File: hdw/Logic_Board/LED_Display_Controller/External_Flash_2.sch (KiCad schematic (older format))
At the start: 16 parts, among them U1901 SST25PF020B

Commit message: Added some digikey partnumbers to components
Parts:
- C1901: footprint (none) -> Capacitors_SMD:C_0603; Digi-Key PN PN -> 311-1344-1-ND; Voltage 25V -> 50V
- C1902: Digi-Key PN PN -> 1276-1921-1-ND; Voltage 25V -> 50V
- C1903: Digi-Key PN PN -> 1276-1018-1-ND; Voltage 25V -> 50V
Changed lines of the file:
@@
 F 0 "C1901" H 5815 5530 50  0000 L CNN
 F 1 "0.1uF" H 5815 5330 50  0000 L CNN
-F 2 "" H 5828 5280 50  0001 C CNN
+F 2 "Capacitors_SMD:C_0603" H 5828 5280 50  0001 C CNN
 F 3 "" H 5815 5530 50  0001 C CNN
 F 4 "0603" H 5640 5530 50  0000 R CNN "display_footprint"
-F 5 "25V" H 5640 5430 50  0000 R CNN "Voltage"
+F 5 "50V" H 5640 5430 50  0000 R CNN "Voltage"
 F 6 "X7R" H 5640 5330 50  0000 R CNN "Dielectric"
-F 7 "PN" H 6215 5930 60  0001 C CNN "Digi-Key PN"
+F 7 "311-1344-1-ND" H 6215 5930 60  0001 C CNN "Digi-Key PN"
 	1    5790 5430
 	1    0    0    -1
@@
 F 3 "" H 6115 5530 50  0001 C CNN
 F 4 "0603" H 5940 5530 50  0001 R CNN "display_footprint"
-F 5 "25V" H 5940 5430 50  0001 R CNN "Voltage"
+F 5 "50V" H 5940 5430 50  0001 R CNN "Voltage"
 F 6 "X7R" H 5940 5330 50  0001 R CNN "Dielectric"
-F 7 "PN" H 6515 5930 60  0001 C CNN "Digi-Key PN"
+F 7 "1276-1921-1-ND" H 6515 5930 60  0001 C CNN "Digi-Key PN"
 	1    6090 5430
 	1    0    0    -1
@@
 F 3 "" H 6415 5530 50  0001 C CNN
 F 4 "0603" H 6240 5530 50  0001 R CNN "display_footprint"
-F 5 "25V" H 6240 5430 50  0001 R CNN "Voltage"
+F 5 "50V" H 6240 5430 50  0001 R CNN "Voltage"
 F 6 "X7R" H 6240 5330 50  0001 R CNN "Dielectric"
-F 7 "PN" H 6815 5930 60  0001 C CNN "Digi-Key PN"
+F 7 "1276-1018-1-ND" H 6815 5930 60  0001 C CNN "Digi-Key PN"
 	1    6390 5430
 	1    0    0    -1

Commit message: Finished first pass of digikey part numbers
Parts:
- R1901, R1902, R1903, R1904, R1905, R1912: Digi-Key PN PN -> A106047CT-ND
- R1906, R1907, R1908, R1909, R1910, R1911: Digi-Key PN PN -> RMCF0603FT10K0CT-ND
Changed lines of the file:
@@
 F 5 "1%" H 5410 4320 50  0000 L CNN "Tolerance"
 F 6 "1/10W" H 5410 4240 50  0000 L CNN "Wattage"
-F 7 "PN" H 5630 4720 60  0001 C CNN "Digi-Key PN"
+F 7 "RMCF0603FT10K0CT-ND" H 5630 4720 60  0001 C CNN "Digi-Key PN"
 	1    5330 4320
 	1    0    0    -1
@@
 F 5 "1%" H 4600 4320 50  0000 L CNN "Tolerance"
 F 6 "1/10W" H 4600 4240 50  0000 L CNN "Wattage"
-F 7 "PN" H 4820 4720 60  0001 C CNN "Digi-Key PN"
+F 7 "RMCF0603FT10K0CT-ND" H 4820 4720 60  0001 C CNN "Digi-Key PN"
 	1    4520 4320
 	1    0    0    -1
@@
 F 5 "1%" H 5190 3130 50  0000 L CNN "Tolerance"
 F 6 "1/10W" H 5190 3050 50  0000 L CNN "Wattage"
-F 7 "PN" H 5410 3530 60  0001 C CNN "Digi-Key PN"
+F 7 "RMCF0603FT10K0CT-ND" H 5410 3530 60  0001 C CNN "Digi-Key PN"
 	1    5110 3130
 	1    0    0    -1
@@
 F 5 "1%" H 4600 3130 50  0000 L CNN "Tolerance"
 F 6 "1/10W" H 4600 3050 50  0000 L CNN "Wattage"
-F 7 "PN" H 4820 3530 60  0001 C CNN "Digi-Key PN"
+F 7 "RMCF0603FT10K0CT-ND" H 4820 3530 60  0001 C CNN "Digi-Key PN"
 	1    4520 3130
 	1    0    0    -1
@@
 F 5 "1%" H 4010 3130 50  0000 L CNN "Tolerance"
 F 6 "1/10W" H 4010 3050 50  0000 L CNN "Wattage"
-F 7 "PN" H 4230 3530 60  0001 C CNN "Digi-Key PN"
+F 7 "RMCF0603FT10K0CT-ND" H 4230 3530 60  0001 C CNN "Digi-Key PN"
 	1    3930 3130
 	1    0    0    -1
@@
 F 5 "1%" H 6830 3850 50  0000 L CNN "Tolerance"
 F 6 "1/10W" H 6830 3770 50  0000 L CNN "Wattage"
-F 7 "PN" H 7050 4250 60  0001 C CNN "Digi-Key PN"
+F 7 "RMCF0603FT10K0CT-ND" H 7050 4250 60  0001 C CNN "Digi-Key PN"
 	1    6750 3850
 	1    0    0    -1
@@
 F 5 "1%" V 3620 3450 50  0001 C CNN "Tolerance"
 F 6 "1/10W" V 3720 3450 50  0001 C CNN "Wattage"
-F 7 "PN" H 3720 3850 60  0001 C CNN "Digi-Key PN"
+F 7 "A106047CT-ND" H 3720 3850 60  0001 C CNN "Digi-Key PN"
 	1    3420 3450
 	0    1    1    0
@@
 F 5 "1%" V 7330 3450 50  0001 C CNN "Tolerance"
 F 6 "1/10W" V 7430 3450 50  0001 C CNN "Wattage"
-F 7 "PN" H 7430 3850 60  0001 C CNN "Digi-Key PN"
+F 7 "A106047CT-ND" H 7430 3850 60  0001 C CNN "Digi-Key PN"
 	1    7130 3450
 	0    1    1    0
@@
 F 5 "1%" V 3620 3550 50  0001 C CNN "Tolerance"
 F 6 "1/10W" V 3720 3550 50  0001 C CNN "Wattage"
-F 7 "PN" H 3720 3950 60  0001 C CNN "Digi-Key PN"
+F 7 "A106047CT-ND" H 3720 3950 60  0001 C CNN "Digi-Key PN"
 	1    3420 3550
 	0    1    1    0
@@
 F 5 "1%" V 3620 3750 50  0001 C CNN "Tolerance"
 F 6 "1/10W" V 3720 3750 50  0001 C CNN "Wattage"
-F 7 "PN" H 3720 4150 60  0001 C CNN "Digi-Key PN"
+F 7 "A106047CT-ND" H 3720 4150 60  0001 C CNN "Digi-Key PN"
 	1    3420 3750
 	0    1    1    0
@@
 F 5 "1%" V 3620 3850 50  0001 C CNN "Tolerance"
 F 6 "1/10W" V 3720 3850 50  0001 C CNN "Wattage"
-F 7 "PN" H 3720 4250 60  0001 C CNN "Digi-Key PN"
+F 7 "A106047CT-ND" H 3720 4250 60  0001 C CNN "Digi-Key PN"
 	1    3420 3850
 	0    1    1    0
@@
 F 5 "1%" V 3620 3650 50  0001 C CNN "Tolerance"
 F 6 "1/10W" V 3720 3650 50  0001 C CNN "Wattage"
-F 7 "PN" H 3720 4050 60  0001 C CNN "Digi-Key PN"
+F 7 "A106047CT-ND" H 3720 4050 60  0001 C CNN "Digi-Key PN"
 	1    3420 3650
 	0    1    1    0

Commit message: First pass assignment of footprints to all components
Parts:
- C1902, C1903: footprint (none) -> Capacitors_SMD:C_0603
- R1901, R1902, R1903, R1904, R1905, R1906, R1907, R1908, R1909, R1910, R1911, R1912: footprint (none) -> Resistors_SMD:R_0603
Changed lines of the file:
@@
 F 0 "R1910" H 5270 4320 50  0000 R CNN
 F 1 "10k" V 5330 4320 50  0000 C CNN
-F 2 "" H 5330 4320 50  0001 C CNN
+F 2 "Resistors_SMD:R_0603" H 5330 4320 50  0001 C CNN
 F 3 "" H 5330 4320 50  0001 C CNN
 F 4 "0603" H 5410 4400 50  0000 L CNN "display_footprint"
@@
 F 0 "R1908" H 4460 4320 50  0000 R CNN
 F 1 "10k" V 4520 4320 50  0000 C CNN
-F 2 "" H 4520 4320 50  0001 C CNN
+F 2 "Resistors_SMD:R_0603" H 4520 4320 50  0001 C CNN
 F 3 "" H 4520 4320 50  0001 C CNN
 F 4 "0603" H 4600 4400 50  0000 L CNN "display_footprint"
@@
 F 0 "R1909" H 5050 3130 50  0000 R CNN
 F 1 "10k" V 5110 3130 50  0000 C CNN
-F 2 "" H 5110 3130 50  0001 C CNN
+F 2 "Resistors_SMD:R_0603" H 5110 3130 50  0001 C CNN
 F 3 "" H 5110 3130 50  0001 C CNN
 F 4 "0603" H 5190 3210 50  0000 L CNN "display_footprint"
@@
 F 0 "R1907" H 4460 3130 50  0000 R CNN
 F 1 "10k" V 4520 3130 50  0000 C CNN
-F 2 "" H 4520 3130 50  0001 C CNN
+F 2 "Resistors_SMD:R_0603" H 4520 3130 50  0001 C CNN
 F 3 "" H 4520 3130 50  0001 C CNN
 F 4 "0603" H 4600 3210 50  0000 L CNN "display_footprint"
@@
 F 0 "R1906" H 3870 3130 50  0000 R CNN
 F 1 "10k" V 3930 3130 50  0000 C CNN
-F 2 "" H 3930 3130 50  0001 C CNN
+F 2 "Resistors_SMD:R_0603" H 3930 3130 50  0001 C CNN
 F 3 "" H 3930 3130 50  0001 C CNN
 F 4 "0603" H 4010 3210 50  0000 L CNN "display_footprint"
@@
 F 0 "R1911" H 6690 3850 50  0000 R CNN
 F 1 "10k" V 6750 3850 50  0000 C CNN
-F 2 "" H 6750 3850 50  0001 C CNN
+F 2 "Resistors_SMD:R_0603" H 6750 3850 50  0001 C CNN
 F 3 "" H 6750 3850 50  0001 C CNN
 F 4 "0603" H 6830 3930 50  0000 L CNN "display_footprint"
@@
 F 0 "R1901" V 3380 3580 50  0000 L CNN
 F 1 "100" V 3420 3450 50  0000 C CNN
-F 2 "" H 3420 3450 50  0001 C CNN
+F 2 "Resistors_SMD:R_0603" H 3420 3450 50  0001 C CNN
 F 3 "" H 3420 3450 50  0001 C CNN
 F 4 "0603" V 3520 3450 50  0001 C CNN "display_footprint"
@@
 F 0 "R1912" V 7030 3450 50  0000 C CNN
 F 1 "100" V 7130 3450 50  0000 C CNN
-F 2 "" H 7130 3450 50  0001 C CNN
+F 2 "Resistors_SMD:R_0603" H 7130 3450 50  0001 C CNN
 F 3 "" H 7130 3450 50  0001 C CNN
 F 4 "0603" V 7230 3450 50  0001 C CNN "display_footprint"
@@
 F 0 "C1902" H 6115 5530 50  0000 L CNN
 F 1 "10nF" H 6115 5330 50  0000 L CNN
-F 2 "" H 6128 5280 50  0001 C CNN
+F 2 "Capacitors_SMD:C_0603" H 6128 5280 50  0001 C CNN
 F 3 "" H 6115 5530 50  0001 C CNN
 F 4 "0603" H 5940 5530 50  0001 R CNN "display_footprint"
@@
 F 0 "C1903" H 6415 5530 50  0000 L CNN
 F 1 "1nF" H 6415 5330 50  0000 L CNN
-F 2 "" H 6428 5280 50  0001 C CNN
+F 2 "Capacitors_SMD:C_0603" H 6428 5280 50  0001 C CNN
 F 3 "" H 6415 5530 50  0001 C CNN
 F 4 "0603" H 6240 5530 50  0001 R CNN "display_footprint"
@@
 F 0 "R1902" V 3380 3680 50  0000 L CNN
 F 1 "100" V 3420 3550 50  0000 C CNN
-F 2 "" H 3420 3550 50  0001 C CNN
+F 2 "Resistors_SMD:R_0603" H 3420 3550 50  0001 C CNN
 F 3 "" H 3420 3550 50  0001 C CNN
 F 4 "0603" V 3520 3550 50  0001 C CNN "display_footprint"
@@
 F 0 "R1904" V 3380 3880 50  0000 L CNN
 F 1 "100" V 3420 3750 50  0000 C CNN
-F 2 "" H 3420 3750 50  0001 C CNN
+F 2 "Resistors_SMD:R_0603" H 3420 3750 50  0001 C CNN
 F 3 "" H 3420 3750 50  0001 C CNN
 F 4 "0603" V 3520 3750 50  0001 C CNN "display_footprint"
@@
 F 0 "R1905" V 3380 3980 50  0000 L CNN
 F 1 "100" V 3420 3850 50  0000 C CNN
-F 2 "" H 3420 3850 50  0001 C CNN
+F 2 "Resistors_SMD:R_0603" H 3420 3850 50  0001 C CNN
 F 3 "" H 3420 3850 50  0001 C CNN
 F 4 "0603" V 3520 3850 50  0001 C CNN "display_footprint"
@@
 F 0 "R1903" V 3380 3780 50  0000 L CNN
 F 1 "100" V 3420 3650 50  0000 C CNN
-F 2 "" H 3420 3650 50  0001 C CNN
+F 2 "Resistors_SMD:R_0603" H 3420 3650 50  0001 C CNN
 F 3 "" H 3420 3650 50  0001 C CNN
 F 4 "0603" V 3520 3650 50  0001 C CNN "display_footprint"

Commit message: Resolved a few library dependencies
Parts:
- R1901, R1902, R1903, R1904, R1905, R1906, R1907, R1908, R1909, R1910, R1911, R1912: symbol Custom_Library:R_Custom -> LED_Display_Local_Library:R_Custom
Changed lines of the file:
@@
 $EndComp
 $Comp
-L Custom_Library:R_Custom R?
+L LED_Display_Local_Library:R_Custom R?
 U 1 1 5BBE78FD
 P 5330 4320
@@
 $EndComp
 $Comp
-L Custom_Library:R_Custom R?
+L LED_Display_Local_Library:R_Custom R?
 U 1 1 5BBE7908
 P 4520 4320
@@
 $EndComp
 $Comp
-L Custom_Library:R_Custom R?
+L LED_Display_Local_Library:R_Custom R?
 U 1 1 5BBE7913
 P 5110 3130
@@
 $EndComp
 $Comp
-L Custom_Library:R_Custom R?
+L LED_Display_Local_Library:R_Custom R?
 U 1 1 5BBE791E
 P 4520 3130
@@
 $EndComp
 $Comp
-L Custom_Library:R_Custom R?
+L LED_Display_Local_Library:R_Custom R?
 U 1 1 5BBE7929
 P 3930 3130
@@
 $EndComp
 $Comp
-L Custom_Library:R_Custom R?
+L LED_Display_Local_Library:R_Custom R?
 U 1 1 5BBE7934
 P 6750 3850
@@
 $EndComp
 $Comp
-L Custom_Library:R_Custom R?
+L LED_Display_Local_Library:R_Custom R?
 U 1 1 5BBE7963
 P 3420 3450
@@
 FLASH_SCK
 $Comp
-L Custom_Library:R_Custom R?
+L LED_Display_Local_Library:R_Custom R?
 U 1 1 5BBE7990
 P 7130 3450
@@
 	6090 5240 6390 5240
 $Comp
-L Custom_Library:R_Custom R?
+L LED_Display_Local_Library:R_Custom R?
 U 1 1 5BBE79DB
 P 3420 3550
@@
 $EndComp
 $Comp
-L Custom_Library:R_Custom R?
+L LED_Display_Local_Library:R_Custom R?
 U 1 1 5BBE79E6
 P 3420 3750
@@
 $EndComp
 $Comp
-L Custom_Library:R_Custom R?
+L LED_Display_Local_Library:R_Custom R?
 U 1 1 5BBE79F1
 P 3420 3850
@@
 ~FLASH_Hold
 $Comp
-L Custom_Library:R_Custom R1903
+L LED_Display_Local_Library:R_Custom R1903
 U 1 1 5BC1C038
 P 3420 3650

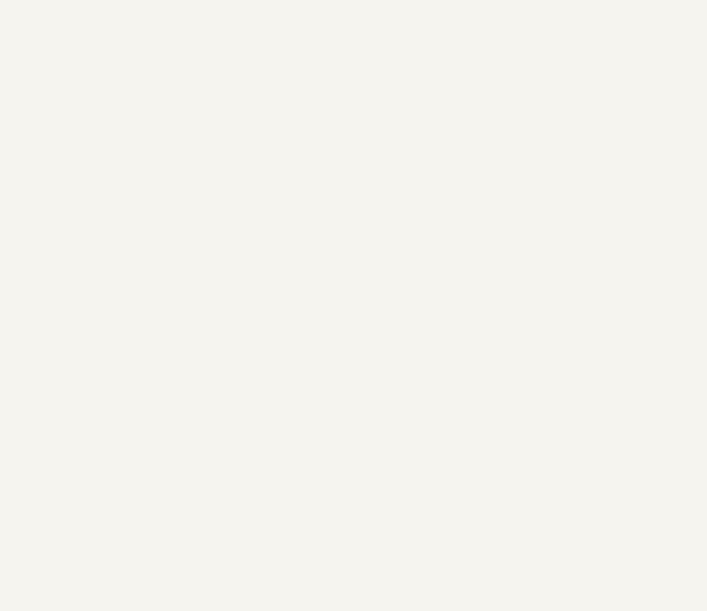
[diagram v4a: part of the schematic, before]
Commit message: Added flash chip select LEDs
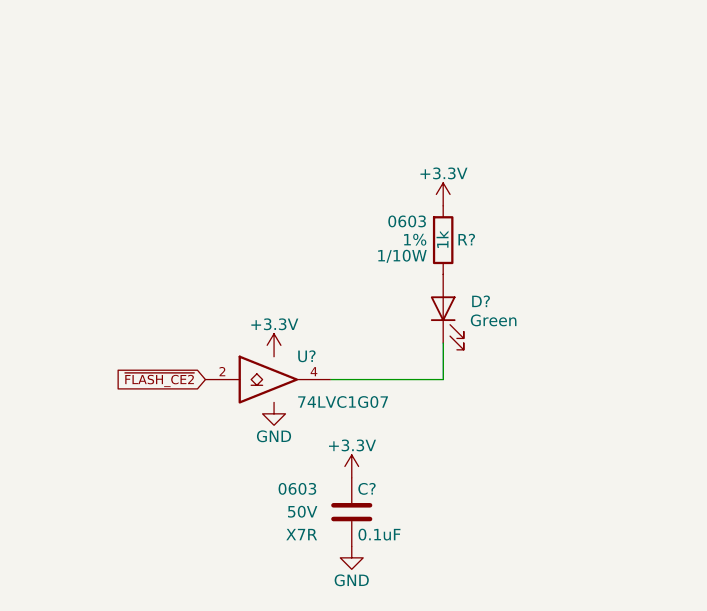
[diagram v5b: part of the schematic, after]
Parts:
- added C?: 0.1uF, Capacitors_SMD:C_0603, symbol LED_Display_Local_Library:C_Custom
- added D?: Green, LEDs:LED_0603, symbol Device:LED
- added R?: 1k, Resistors_SMD:R_0603, symbol LED_Display_Local_Library:R_Custom
- added U?: 74LVC1G07, TO_SOT_Packages_SMD:SOT-353_SC-70-5, symbol LED_Display_Local_Library:74LVC1G07_Power
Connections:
- net +3V3: now also C?.1, R?.1, U?.5 (VCC)
- net GND: now also C?.2, U?.3 (GND)
- net ~FLASH_CE2: now also U?.2
- new net: D?.1 (K), U?.4
- new net: D?.2 (A), R?.2
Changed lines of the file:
@@
 Wire Wire Line
 	4520 3850 5680 3850
+$Comp
+L LED_Display_Local_Library:C_Custom C?
+U 1 1 5C17189B
+P 2010 6900
+AR Path="/5BAAE16C/5C17189B" Ref="C?"  Part="1"
+AR Path="/5BB181D8/5C17189B" Ref="C?"  Part="1"
+AR Path="/5BB2595E/5C17189B" Ref="C?"  Part="1"
+AR Path="/5BB25AE7/5C17189B" Ref="C?"  Part="1"
+F 0 "C?" H 2035 7000 50  0000 L CNN
+F 1 "0.1uF" H 2035 6800 50  0000 L CNN
+F 2 "Capacitors_SMD:C_0603" H 2048 6750 50  0001 C CNN
+F 3 "" H 2035 7000 50  0001 C CNN
+F 4 "0603" H 1860 7000 50  0000 R CNN "display_footprint"
+F 5 "50V" H 1860 6900 50  0000 R CNN "Voltage"
+F 6 "X7R" H 1860 6800 50  0000 R CNN "Dielectric"
+F 7 "311-1344-1-ND" H 2435 7400 60  0001 C CNN "Digi-Key PN"
+	1    2010 6900
+	1    0    0    -1
+$EndComp
+$Comp
+L LED_Display_Local_Library:74LVC1G07_Power U?
+U 1 1 5C1718A3
+P 1670 6320
+AR Path="/5BB2595E/5C1718A3" Ref="U?"  Part="1"
+AR Path="/5BB25AE7/5C1718A3" Ref="U?"  Part="1"
+F 0 "U?" H 1770 6420 50  0000 L CNN
+F 1 "74LVC1G07" H 1770 6220 50  0000 L CNN
+F 2 "TO_SOT_Packages_SMD:SOT-353_SC-70-5" H 1670 6320 50  0001 C CNN
+F 3 "http://www.ti.com/lit/sg/scyt129e/scyt129e.pdf" H 1670 6320 50  0001 C CNN
+F 4 "296-8486-1-ND" H 1670 6320 50  0001 C CNN "Digi-Key PN"
+	1    1670 6320
+	1    0    0    -1
+$EndComp
+$Comp
+L power:+3.3V #PWR?
+U 1 1 5C1718AA
+P 1670 6220
+AR Path="/5BB2595E/5C1718AA" Ref="#PWR?"  Part="1"
+AR Path="/5BB25AE7/5C1718AA" Ref="#PWR?"  Part="1"
+F 0 "#PWR?" H 1670 6070 50  0001 C CNN
+F 1 "+3.3V" H 1670 6360 50  0000 C CNN
+F 2 "" H 1670 6220 50  0001 C CNN
+F 3 "" H 1670 6220 50  0001 C CNN
+	1    1670 6220
+	1    0    0    -1
+$EndComp
+$Comp
+L power:+3.3V #PWR?
+U 1 1 5C1718B0
+P 2010 6750
+AR Path="/5BB2595E/5C1718B0" Ref="#PWR?"  Part="1"
+AR Path="/5BB25AE7/5C1718B0" Ref="#PWR?"  Part="1"
+F 0 "#PWR?" H 2010 6600 50  0001 C CNN
+F 1 "+3.3V" H 2010 6890 50  0000 C CNN
+F 2 "" H 2010 6750 50  0001 C CNN
+F 3 "" H 2010 6750 50  0001 C CNN
+	1    2010 6750
+	1    0    0    -1
+$EndComp
+$Comp
+L power:GND #PWR?
+U 1 1 5C1718B6
+P 2010 7050
+AR Path="/5BB2595E/5C1718B6" Ref="#PWR?"  Part="1"
+AR Path="/5BB25AE7/5C1718B6" Ref="#PWR?"  Part="1"
+F 0 "#PWR?" H 2010 6800 50  0001 C CNN
+F 1 "GND" H 2010 6900 50  0000 C CNN
+F 2 "" H 2010 7050 50  0001 C CNN
+F 3 "" H 2010 7050 50  0001 C CNN
+	1    2010 7050
+	1    0    0    -1
+$EndComp
+$Comp
+L power:GND #PWR?
+U 1 1 5C1718BC
+P 1670 6420
+AR Path="/5BB2595E/5C1718BC" Ref="#PWR?"  Part="1"
+AR Path="/5BB25AE7/5C1718BC" Ref="#PWR?"  Part="1"
+F 0 "#PWR?" H 1670 6170 50  0001 C CNN
+F 1 "GND" H 1670 6270 50  0000 C CNN
+F 2 "" H 1670 6420 50  0001 C CNN
+F 3 "" H 1670 6420 50  0001 C CNN
+	1    1670 6420
+	1    0    0    -1
+$EndComp
+Text GLabel 1370 6320 0    40   Input ~ 0
+~FLASH_CE2
+$Comp
+L power:+3.3V #PWR?
+U 1 1 5C1718C3
+P 2410 5560
+AR Path="/5BB844FD/5C1718C3" Ref="#PWR?"  Part="1"
+AR Path="/5BF346B3/5C1718C3" Ref="#PWR?"  Part="1"
+AR Path="/5BB2595E/5C1718C3" Ref="#PWR?"  Part="1"
+AR Path="/5BB25AE7/5C1718C3" Ref="#PWR?"  Part="1"
+F 0 "#PWR?" H 2410 5410 50  0001 C CNN
+F 1 "+3.3V" H 2410 5700 50  0000 C CNN
+F 2 "" H 2410 5560 50  0001 C CNN
+F 3 "" H 2410 5560 50  0001 C CNN
+	1    2410 5560
+	1    0    0    -1
+$EndComp
+Wire Wire Line
+	1920 6320 2410 6320
+Wire Wire Line
+	2410 6320 2410 6160
+$Comp
+L LED_Display_Local_Library:R_Custom R?
+U 1 1 5C1718CF
+P 2410 5710
+AR Path="/5BAAE1F3/5C1718CF" Ref="R?"  Part="1"
+AR Path="/5BAAE1DC/5C1718CF" Ref="R?"  Part="1"
+AR Path="/5BAAE16C/5C1718CF" Ref="R?"  Part="1"
+AR Path="/5BB844FD/5C1718CF" Ref="R?"  Part="1"
+AR Path="/5BF346B3/5C1718CF" Ref="R?"  Part="1"
+AR Path="/5BB2595E/5C1718CF" Ref="R?"  Part="1"
+AR Path="/5BB25AE7/5C1718CF" Ref="R?"  Part="1"
+F 0 "R?" H 2350 5710 50  0000 R CNN
+F 1 "1k" V 2410 5710 50  0000 C CNN
+F 2 "Resistors_SMD:R_0603" H 2410 5710 50  0001 C CNN
+F 3 "" H 2410 5710 50  0001 C CNN
+F 4 "0603" H 2480 5790 50  0000 L CNN "display_footprint"
+F 5 "1%" H 2480 5710 50  0000 L CNN "Tolerance"
+F 6 "1/10W" H 2480 5640 50  0000 L CNN "Wattage"
+F 7 "RMCF0603FT1K00CT-ND" H 2710 6110 60  0001 C CNN "Digi-Key PN"
+	1    2410 5710
+	-1   0    0    -1
+$EndComp
+$Comp
+L Device:LED D?
+U 1 1 5C1718D7
+P 2410 6010
+AR Path="/5BB844FD/5C1718D7" Ref="D?"  Part="1"
+AR Path="/5BF346B3/5C1718D7" Ref="D?"  Part="1"
+AR Path="/5BB2595E/5C1718D7" Ref="D?"  Part="1"
+AR Path="/5BB25AE7/5C1718D7" Ref="D?"  Part="1"
+F 0 "D?" V 2440 5890 50  0000 R CNN
+F 1 "Green" V 2357 5893 50  0000 R CNN
+F 2 "LEDs:LED_0603" H 2410 6010 50  0001 C CNN
+F 3 "~" H 2410 6010 50  0001 C CNN
+F 4 "160-1446-1-ND" H -2600 3010 50  0001 C CNN "Digi-Key PN"
+	1    2410 6010
+	0    -1   -1   0
+$EndComp
 $EndSCHEMATC

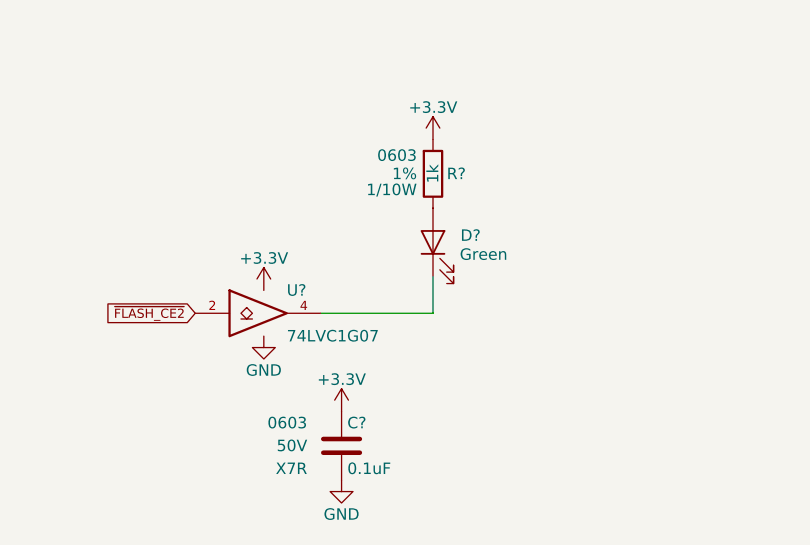
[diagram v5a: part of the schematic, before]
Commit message: Added WIFI comm LED
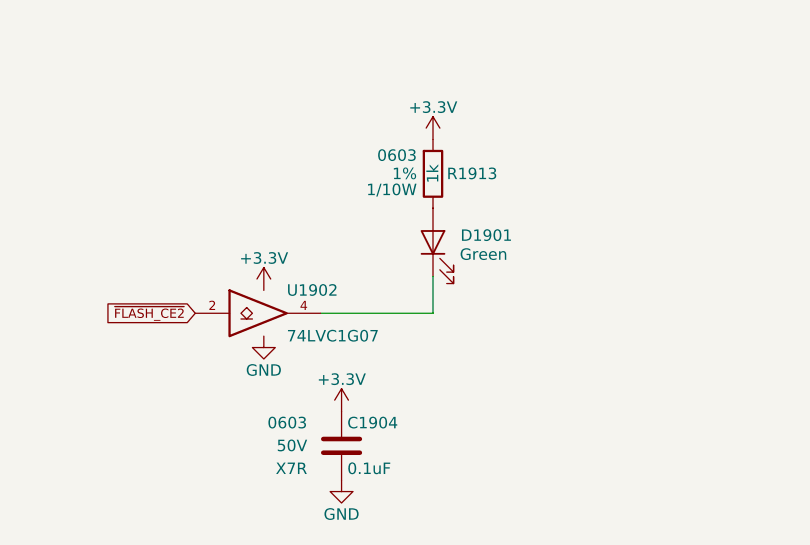
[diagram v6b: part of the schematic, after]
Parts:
- gave numbers to parts that had none: 4
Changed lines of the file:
@@
 AR Path="/5BB181D8/5C17189B" Ref="C?"  Part="1"
 AR Path="/5BB2595E/5C17189B" Ref="C?"  Part="1"
-AR Path="/5BB25AE7/5C17189B" Ref="C?"  Part="1"
-F 0 "C?" H 2035 7000 50  0000 L CNN
+AR Path="/5BB25AE7/5C17189B" Ref="C1904"  Part="1"
+F 0 "C1904" H 2035 7000 50  0000 L CNN
 F 1 "0.1uF" H 2035 6800 50  0000 L CNN
 F 2 "Capacitors_SMD:C_0603" H 2048 6750 50  0001 C CNN
@@
 P 1670 6320
 AR Path="/5BB2595E/5C1718A3" Ref="U?"  Part="1"
-AR Path="/5BB25AE7/5C1718A3" Ref="U?"  Part="1"
-F 0 "U?" H 1770 6420 50  0000 L CNN
+AR Path="/5BB25AE7/5C1718A3" Ref="U1902"  Part="1"
+F 0 "U1902" H 1770 6420 50  0000 L CNN
 F 1 "74LVC1G07" H 1770 6220 50  0000 L CNN
 F 2 "TO_SOT_Packages_SMD:SOT-353_SC-70-5" H 1670 6320 50  0001 C CNN
@@
 P 1670 6220
 AR Path="/5BB2595E/5C1718AA" Ref="#PWR?"  Part="1"
-AR Path="/5BB25AE7/5C1718AA" Ref="#PWR?"  Part="1"
-F 0 "#PWR?" H 1670 6070 50  0001 C CNN
+AR Path="/5BB25AE7/5C1718AA" Ref="#PWR01911"  Part="1"
+F 0 "#PWR01911" H 1670 6070 50  0001 C CNN
 F 1 "+3.3V" H 1670 6360 50  0000 C CNN
 F 2 "" H 1670 6220 50  0001 C CNN
@@
 P 2010 6750
 AR Path="/5BB2595E/5C1718B0" Ref="#PWR?"  Part="1"
-AR Path="/5BB25AE7/5C1718B0" Ref="#PWR?"  Part="1"
-F 0 "#PWR?" H 2010 6600 50  0001 C CNN
+AR Path="/5BB25AE7/5C1718B0" Ref="#PWR01913"  Part="1"
+F 0 "#PWR01913" H 2010 6600 50  0001 C CNN
 F 1 "+3.3V" H 2010 6890 50  0000 C CNN
 F 2 "" H 2010 6750 50  0001 C CNN
@@
 P 2010 7050
 AR Path="/5BB2595E/5C1718B6" Ref="#PWR?"  Part="1"
-AR Path="/5BB25AE7/5C1718B6" Ref="#PWR?"  Part="1"
-F 0 "#PWR?" H 2010 6800 50  0001 C CNN
+AR Path="/5BB25AE7/5C1718B6" Ref="#PWR01914"  Part="1"
+F 0 "#PWR01914" H 2010 6800 50  0001 C CNN
 F 1 "GND" H 2010 6900 50  0000 C CNN
 F 2 "" H 2010 7050 50  0001 C CNN
@@
 P 1670 6420
 AR Path="/5BB2595E/5C1718BC" Ref="#PWR?"  Part="1"
-AR Path="/5BB25AE7/5C1718BC" Ref="#PWR?"  Part="1"
-F 0 "#PWR?" H 1670 6170 50  0001 C CNN
+AR Path="/5BB25AE7/5C1718BC" Ref="#PWR01912"  Part="1"
+F 0 "#PWR01912" H 1670 6170 50  0001 C CNN
 F 1 "GND" H 1670 6270 50  0000 C CNN
 F 2 "" H 1670 6420 50  0001 C CNN
@@
 AR Path="/5BF346B3/5C1718C3" Ref="#PWR?"  Part="1"
 AR Path="/5BB2595E/5C1718C3" Ref="#PWR?"  Part="1"
-AR Path="/5BB25AE7/5C1718C3" Ref="#PWR?"  Part="1"
-F 0 "#PWR?" H 2410 5410 50  0001 C CNN
+AR Path="/5BB25AE7/5C1718C3" Ref="#PWR01915"  Part="1"
+F 0 "#PWR01915" H 2410 5410 50  0001 C CNN
 F 1 "+3.3V" H 2410 5700 50  0000 C CNN
 F 2 "" H 2410 5560 50  0001 C CNN
@@
 AR Path="/5BF346B3/5C1718CF" Ref="R?"  Part="1"
 AR Path="/5BB2595E/5C1718CF" Ref="R?"  Part="1"
-AR Path="/5BB25AE7/5C1718CF" Ref="R?"  Part="1"
-F 0 "R?" H 2350 5710 50  0000 R CNN
+AR Path="/5BB25AE7/5C1718CF" Ref="R1913"  Part="1"
+F 0 "R1913" H 2350 5710 50  0000 R CNN
 F 1 "1k" V 2410 5710 50  0000 C CNN
 F 2 "Resistors_SMD:R_0603" H 2410 5710 50  0001 C CNN
@@
 AR Path="/5BF346B3/5C1718D7" Ref="D?"  Part="1"
 AR Path="/5BB2595E/5C1718D7" Ref="D?"  Part="1"
-AR Path="/5BB25AE7/5C1718D7" Ref="D?"  Part="1"
-F 0 "D?" V 2440 5890 50  0000 R CNN
+AR Path="/5BB25AE7/5C1718D7" Ref="D1901"  Part="1"
+F 0 "D1901" V 2440 5890 50  0000 R CNN
 F 1 "Green" V 2357 5893 50  0000 R CNN
 F 2 "LEDs:LED_0603" H 2410 6010 50  0001 C CNN
